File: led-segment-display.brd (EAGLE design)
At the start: 18 x 30 mm, 56 parts, among them J3 1x3 RA Female .1", U1 AL8805

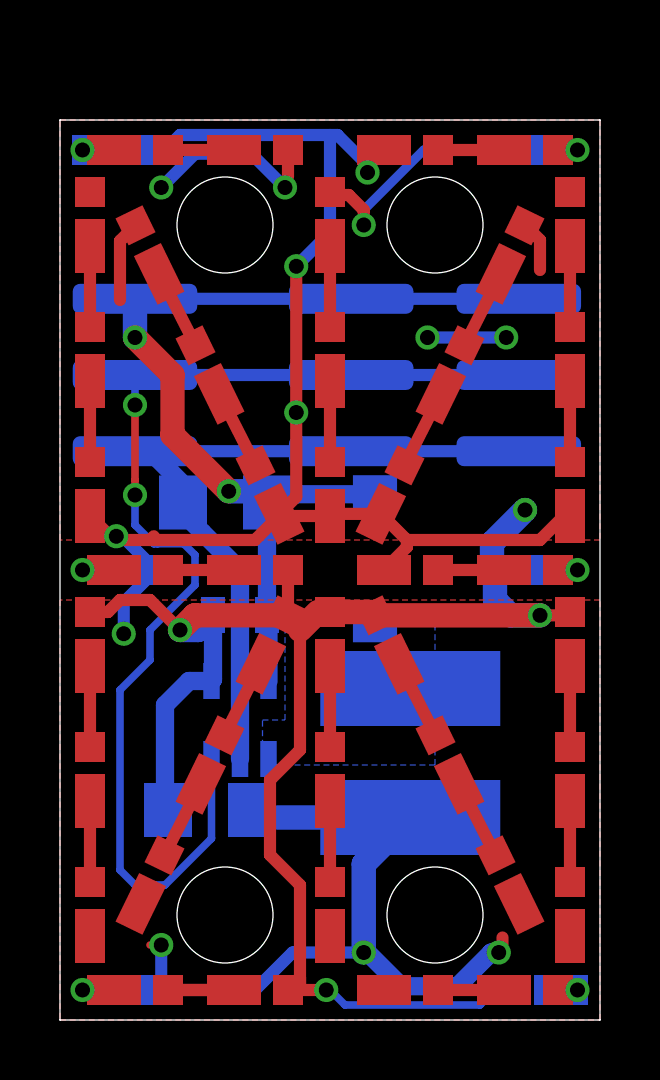
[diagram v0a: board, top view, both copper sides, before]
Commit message: led-segment-display - update led package for easier hand soldering
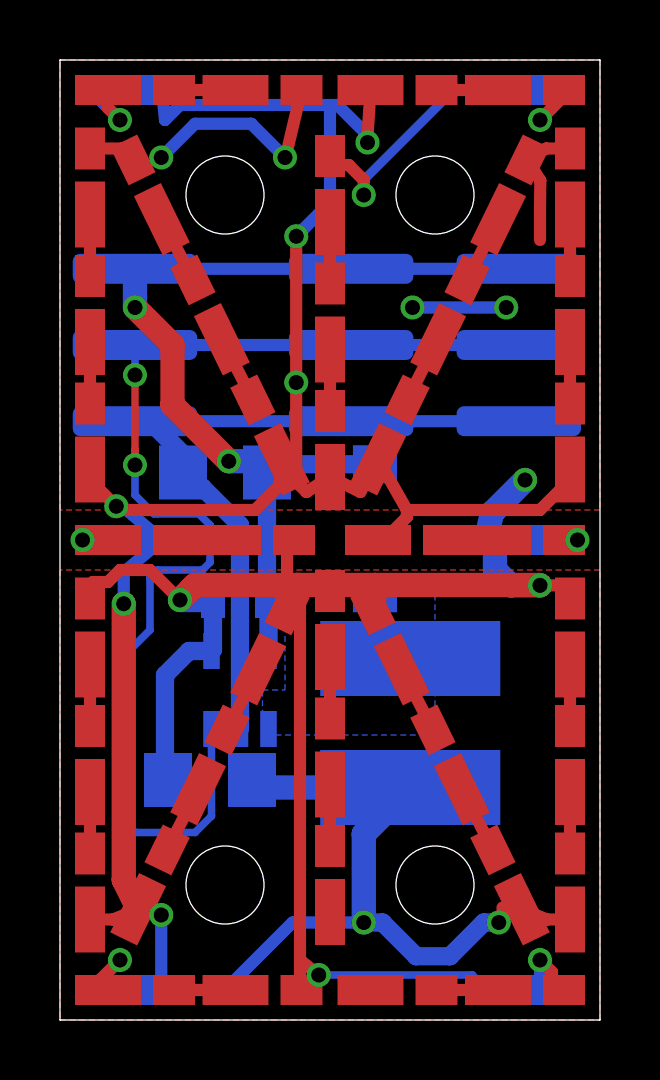
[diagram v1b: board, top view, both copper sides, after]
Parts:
- moved LED44 2.06 mm to (2.50, 31.0)
- moved LED5 2.02 mm to (11.2, 31.0)
- moved LED6 2.02 mm to (6.75, 31.0)
- moved LED28 2.00 mm to (3.00, 27.5)
- moved LED29 2.00 mm to (5.00, 23.5)
- moved LED30 2.00 mm to (15.0, 27.5)
- moved LED31 2.00 mm to (13.0, 23.5)
- moved LED37 2.00 mm to (7.00, 19.5)
- moved LED38 2.00 mm to (11.0, 19.5)
- moved LED4 2.00 mm to (15.5, 31.0)
- moved LED40 2.00 mm to (2.50, 31.0)
- moved LED43 2.00 mm to (15.5, 31.0)
- moved LED3 1.75 mm to (1.00, 19.2)
- moved LED9 1.75 mm to (17.0, 19.2)
- moved LED2 1.50 mm to (1.00, 23.5)
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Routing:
- net I_C: track 72.8 -> 92.2 mm
- net I_A: track 75.5 -> 83.4 mm
- net N$34: track 1.20 -> 2.84 mm
- net N$8: track 1.20 -> 2.50 mm
- net N$12: track 1.70 -> 2.68 mm
- net VIN: track 31.7 -> 32.6 mm
- net N$4: track 1.70 -> 2.50 mm
- net CTRL_CH1: track 38.3 -> 39.0 mm
- net N$9: track 2.70 -> 2.05 mm
- net N$17: track 2.70 -> 2.05 mm
- net N$13: track 2.70 -> 2.05 mm
- net N$18: track 2.70 -> 2.05 mm
- net N$14: track 2.70 -> 2.05 mm
- net N$10: track 2.70 -> 2.05 mm
- net N$6: track 2.70 -> 2.05 mm
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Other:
- board size 18 x 30 mm -> 18 x 32 mm
- board text added: "V1.1"
- board text removed: "V1.0"

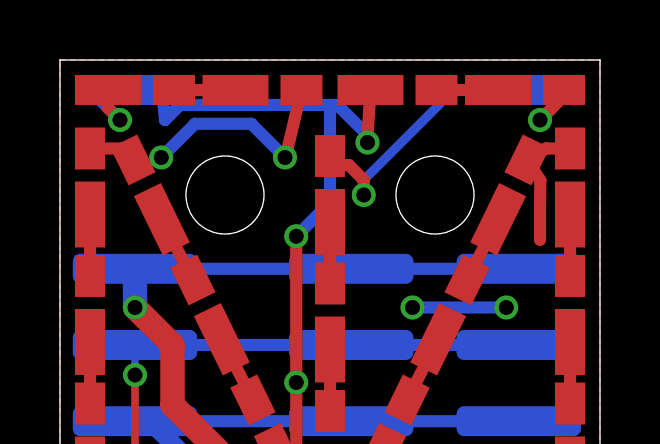
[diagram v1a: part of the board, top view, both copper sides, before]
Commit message: led-segment-display: add TOP marker to front of PCB
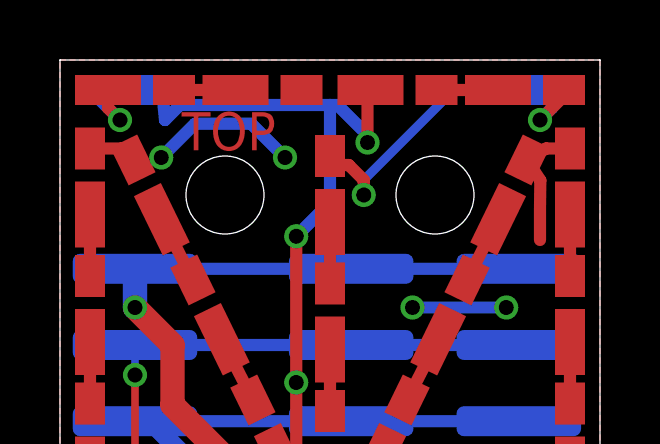
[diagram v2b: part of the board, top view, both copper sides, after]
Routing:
- net I_A: track 83.4 -> 81.5 mm
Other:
- board text added: "TOP"
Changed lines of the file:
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@@
 <text x="6" y="20" size="1.27" layer="26" font="vector" rot="MR180" align="center">GND</text>
 <text x="6" y="22.5" size="1.27" layer="26" font="vector" rot="MR180" align="center">PWM</text>
+<text x="5.625" y="29.625" size="1.27" layer="1" font="vector" ratio="20" align="center">TOP</text>
 </plain>
 <attributes>
@@
 <wire x1="8.625" y1="1.5" x2="8" y2="2" width="0.4064" layer="1"/>
 <wire x1="8" y1="1.05" x2="8" y2="14.5" width="0.4064" layer="1"/>
-<wire x1="8.05" y1="31" x2="7.6" y2="29.1" width="0.4064" layer="1"/>
 <wire x1="14.2" y1="31" x2="13.125" y2="31" width="0.3048" layer="16"/>
 <wire x1="13.125" y1="31" x2="10.125" y2="28" width="0.3048" layer="16"/>
@@
 <via x="10.25" y="29.25" extent="1-16" drill="0.5" shape="octagon"/>
 <wire x1="10.25" y1="29.25" x2="10.25" y2="29.45" width="0.4064" layer="1"/>
-<wire x1="10.25" y1="29.45" x2="10.35" y2="31" width="0.4064" layer="1"/>
 <wire x1="10.75" y1="3.25" x2="10.125" y2="3.25" width="0.6096" layer="16"/>
 <wire x1="10.125" y1="3.25" x2="7.75" y2="3.25" width="0.4064" layer="16"/>
@@
 <wire x1="1" y1="18.35" x2="1" y2="18" width="0.4064" layer="1"/>
 <wire x1="1" y1="18" x2="1.875" y2="17.125" width="0.4064" layer="1"/>
+<wire x1="10.25" y1="29.45" x2="10.25" y2="30.9" width="0.4064" layer="1"/>
+<wire x1="10.25" y1="30.9" x2="10.35" y2="31" width="0.4064" layer="1"/>
 </signal>
 <signal name="GND">
